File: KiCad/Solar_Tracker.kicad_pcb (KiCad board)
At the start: 2 copper layers, 160 x 100 mm, 116 parts, among them J1 +48V, J10 AZJMP, J11 ELJMP, J12 AZ, J13 CONN_01X03, J2 HOLE, J3 HOLE, J4 EL, J5 HOLE, J6 HOLE, J7 CONN_01X05, J8 GPIO, J9 GPIO, Q1 BUK9M42-60E, Q2 BUK9M42-60E, Q3 BUK9M42-60E, Q4 BUK9M42-60E, Q5 BUK9M42-60E, Q6 BUK9M42-60E, Q7 BUK9M42-60E, Q8 BUK9M42-60E, U1 MER1S4805SC, U10 TLP291, U11 75LBC182, U12 A4927, U2 A4927, U3 Nano, U4 A4927, U5 A4927, U6 MER1S4805SC, U7 TLP291, U8 TLP291, U9 TLP291

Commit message: Imported netlist
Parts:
- U12, U2, U4, U5: footprint Housings_SSOP:ST_PowerSSO-24_SlugDown_ThermalVias -> SOLAR:TSSOP-24_4.4x7.8mm_Pitch0.65mm
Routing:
- net GND: track 160.9 -> 142.9 mm
- net (no net): track 183.3 -> 192.8 mm
- net Net-(U5-Pad14): track 0.00 -> 3.21 mm
- net Net-(U2-Pad14): track 0.00 -> 2.20 mm
- net Net-(U12-Pad14): track 0.00 -> 1.56 mm
- net Net-(U4-Pad14): track 0.00 -> 1.43 mm

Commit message: Fixed connectors
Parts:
- J1, J12, J4, J8, J9: footprint Connectors_Phoenix:PhoenixContact_GMSTBA-G_02x7.50mm_Angled -> Connectors_Phoenix:PhoenixContact_GMSTBVA-G_02x7.50mm_Vertical
- J13: footprint Connectors_Phoenix:PhoenixContact_GMSTBA-G_03x7.50mm_Angled -> Connectors_Phoenix:PhoenixContact_MCV-G_03x5.08mm_Vertical
- J7: footprint Connectors_Phoenix:PhoenixContact_GMSTBA-G_05x7.50mm_Angled -> Connectors_Phoenix:PhoenixContact_MCV-G_05x5.08mm_Vertical
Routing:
- net GND: track 142.9 -> 156.3 mm
- net A7: track 63.6 -> 50.2 mm

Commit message: Added expander to pcb
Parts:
- added C33: 1u, Capacitors_SMD:C_1206_HandSoldering, F.Cu at (69.8, 133.3)
- added R33: 1K, Resistors_SMD:R_1206_HandSoldering, F.Cu at (78.7, 128.3)
- added R34: 1K, Resistors_SMD:R_1206_HandSoldering, F.Cu at (78.7, 121.9)
- added R37: 1K, Resistors_SMD:R_1206_HandSoldering, F.Cu at (78.7, 115.6)
- added R38: 1K, Resistors_SMD:R_1206_HandSoldering, F.Cu at (88.9, 116.8)
- added R42: 1K, Resistors_SMD:R_1206_HandSoldering, F.Cu at (87.6, 121.9)
- added U13: PCA9685, Housings_SSOP:TSSOP-28_4.4x9.7mm_Pitch0.65mm, F.Cu at (66.0, 121.9)
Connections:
- U3 pad 11: ELBL -> Net-(U3-Pad11)
- U3 pad 12: ELBH -> Net-(U3-Pad12)
- U3 pad 13: AZBL -> Net-(U3-Pad13)
- U3 pad 14: AZBH -> Net-(U3-Pad14)
- U3 pad 23: TLED -> Net-(R34-Pad2)
- U3 pad 24: RLED -> Net-(U13-Pad26)
- U3 pad 5: AZFL -> Net-(U3-Pad5)
- U3 pad 6: AZFH -> Net-(U3-Pad6)
- U3 pad 7: ELFL -> Net-(U3-Pad7)
- U3 pad 8: ELFH -> Net-(U3-Pad8)
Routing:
- net Net-(U3-Pad14): track 0.00 -> 195.2 mm
- net AZBH: track 195.2 -> 0.00 mm
- net Net-(U3-Pad13): track 0.00 -> 190.4 mm
- net AZBL: track 190.4 -> 0.00 mm
- net Net-(U3-Pad12): track 0.00 -> 158.8 mm
- net ELBH: track 158.8 -> 0.00 mm
- net Net-(U3-Pad11): track 0.00 -> 154.1 mm
- net ELBL: track 154.1 -> 0.00 mm
- net Net-(U3-Pad8): track 0.00 -> 43.7 mm
- net ELFH: track 43.7 -> 0.00 mm
- net Net-(U3-Pad7): track 0.00 -> 42.1 mm
- net ELFL: track 42.1 -> 0.00 mm
- net Net-(U3-Pad6): track 0.00 -> 41.7 mm
- net AZFH: track 41.7 -> 0.00 mm
- net Net-(U3-Pad5): track 0.00 -> 38.8 mm
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
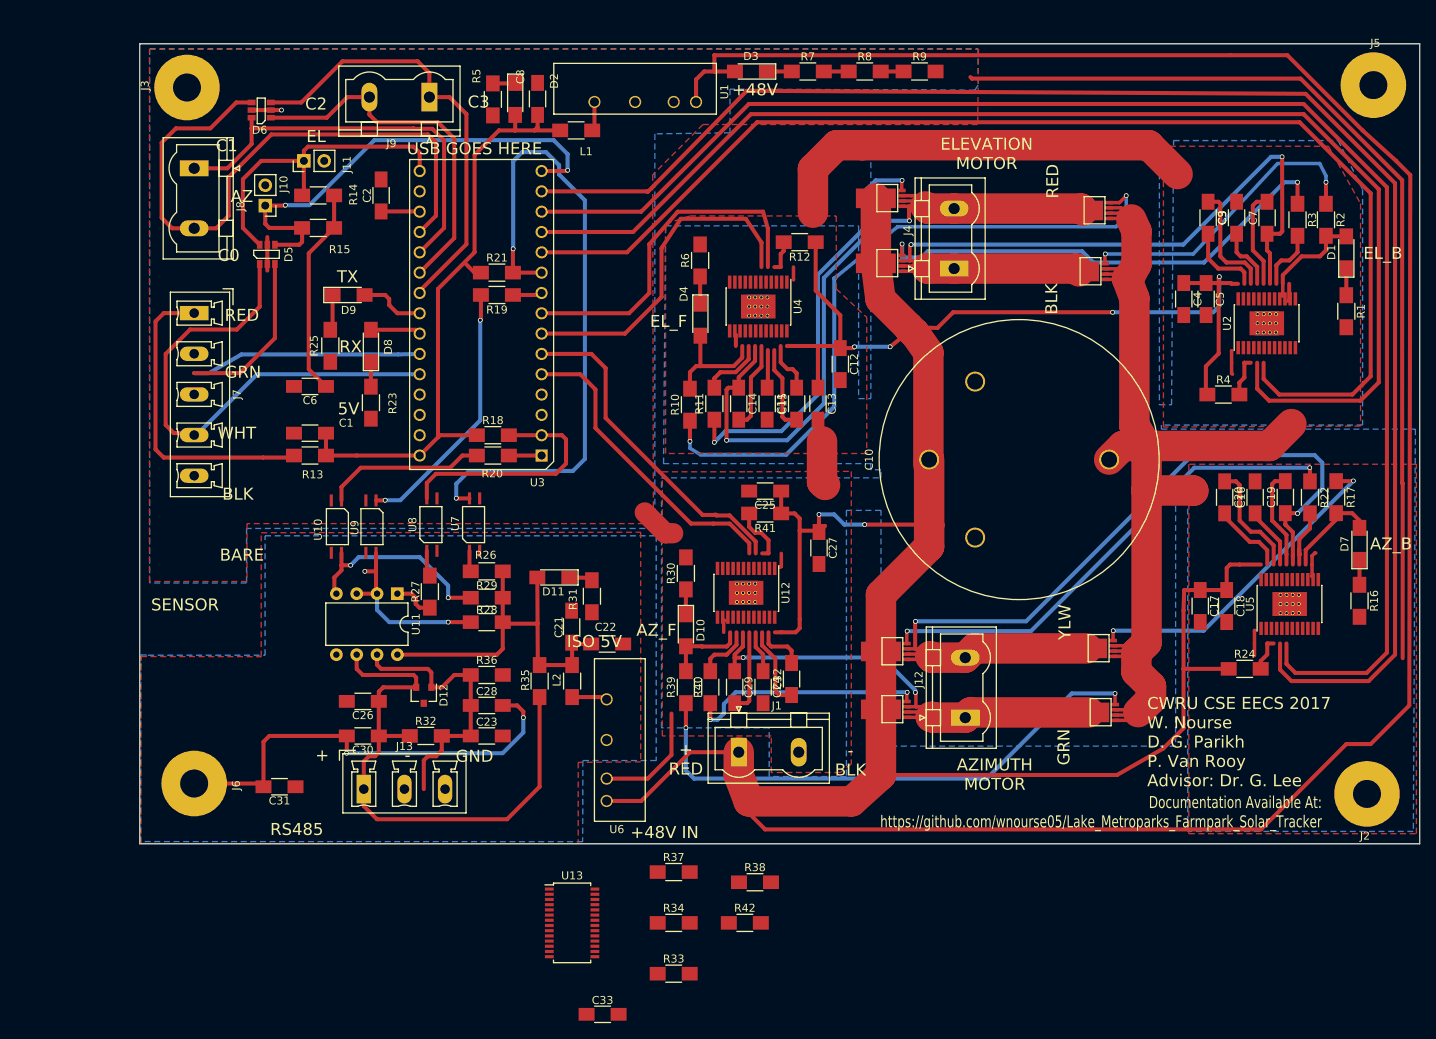
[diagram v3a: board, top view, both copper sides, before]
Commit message: updates to layout due to new footprints. Gave space to power, fixed connectors, began motors
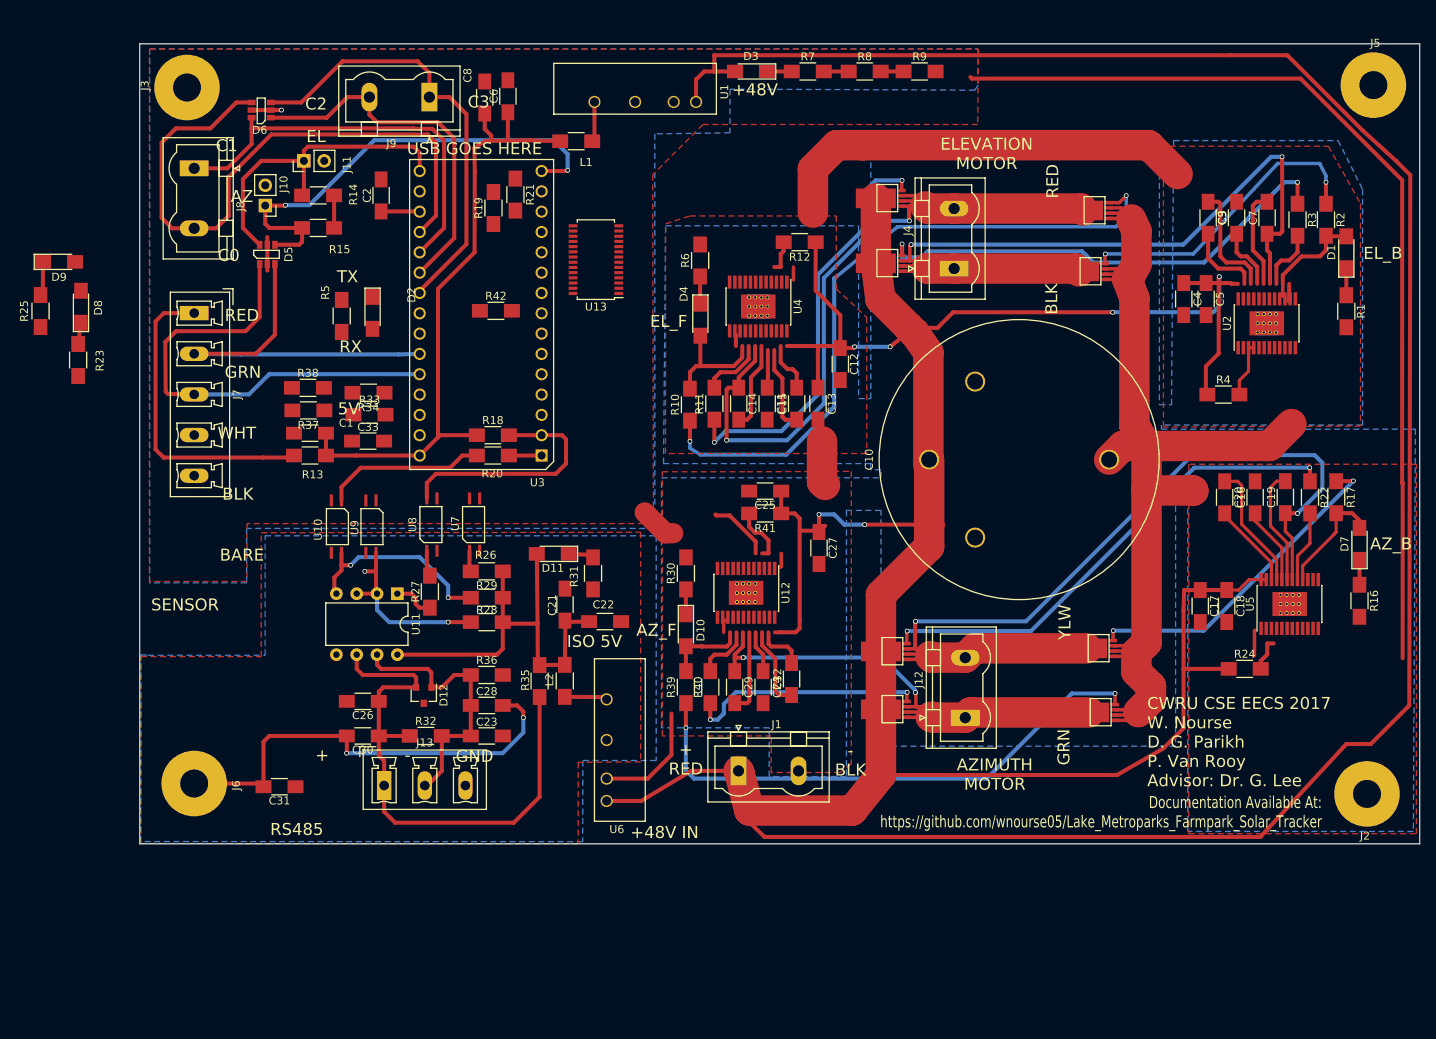
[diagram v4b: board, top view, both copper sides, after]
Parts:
- moved R38 83.3 mm to (33.0, 55.0)
- moved U13 83.0 mm to (69.0, 39.0), turned to 180 degrees
- moved R42 82.6 mm to (56.5, 45.4)
- moved R33 79.6 mm to (40.7, 58.4)
- moved C33 77.4 mm to (40.5, 61.7)
- moved R34 76.5 mm to (40.6, 55.7), turned to 180 degrees
- moved R37 73.6 mm to (33.1, 57.9), turned to 180 degrees
- moved C6 43.9 mm to (58.0, 18.6), turned to 90 degrees
- moved R23 37.0 mm to (4.29, 51.6)
- moved D8 36.6 mm to (4.65, 44.9)
- moved R25 36.5 mm to (-0.41, 45.4)
- moved D9 36.4 mm to (1.91, 39.3)
- moved R5 33.0 mm to (37.2, 46.1)
- moved D2 32.1 mm to (41.1, 45.7)
- moved R19 10.9 mm to (56.2, 32.6), turned to 90 degrees
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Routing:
- net Net-(U3-Pad14): track 195.2 -> 0.00 mm
- net Net-(U3-Pad13): track 190.4 -> 0.00 mm
- net Net-(U3-Pad12): track 158.8 -> 0.00 mm
- net Net-(U3-Pad11): track 154.1 -> 0.00 mm
- net ISO_PWR_DET: track 83.3 -> 0.00 mm, vias 2 -> 0
- net Net-(U3-Pad8): track 43.7 -> 0.00 mm
- net Net-(U3-Pad7): track 42.1 -> 0.00 mm
- net Net-(U3-Pad6): track 41.7 -> 0.00 mm
- net Net-(U3-Pad5): track 38.8 -> 0.00 mm
- net Net-(R19-Pad2): track 32.9 -> 0.00 mm, vias 2 -> 0
- net +5V: track 104.3 -> 83.1 mm
- net GND: track 156.3 -> 143.4 mm
- net A7: track 50.2 -> 58.9 mm
- net +48V: track 613.7 -> 606.7 mm
- net RLED: track 5.62 -> 0.00 mm
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
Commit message: continued with motors and new layout
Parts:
- moved D2 13.1 mm to (30.2, 52.9), turned to 0 degrees
- moved R5 12.0 mm to (30.2, 55.8), turned to 0 degrees
- moved R37 12.0 mm to (40.3, 48.3), turned to 0 degrees
- moved R42 11.6 mm to (55.9, 57.0)
- moved R19 10.5 mm to (57.0, 43.1), turned to 180 degrees
- moved R21 9.62 mm to (58.0, 40.5), turned to 0 degrees
- moved R38 7.74 mm to (40.5, 52.9), turned to 180 degrees
- moved U13 3.36 mm to (69.8, 35.8)
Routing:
- net Net-(R34-Pad2): track 0.00 -> 93.8 mm, vias 0 -> 4
- net Net-(U13-Pad26): track 0.00 -> 85.6 mm, vias 0 -> 1
- net +5V: track 83.1 -> 139.7 mm
- net Net-(R42-Pad2): track 0.00 -> 48.6 mm, vias 0 -> 2
- net GND: track 143.4 -> 188.2 mm
- net ISO_PWR_DET: track 0.00 -> 39.1 mm, vias 0 -> 2
- net Net-(R19-Pad2): track 0.00 -> 35.0 mm, vias 0 -> 2
- net (no net): track 197.8 -> 173.0 mm
- net AZRTE: track 59.6 -> 53.7 mm
- net Net-(R37-Pad2): track 0.00 -> 4.66 mm
- net EN: track 0.00 -> 3.27 mm
- net Net-(D2-Pad1): track 0.00 -> 2.92 mm
- net Net-(R33-Pad2): track 0.00 -> 2.80 mm
- net Net-(C15-Pad1): track 10.7 -> 13.4 mm
- net Net-(C11-Pad1): track 4.74 -> 7.15 mm
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
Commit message: Same stuff, different day
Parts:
- removed D8: RX, LEDs:LED_1206_HandSoldering
- removed D9: TX, LEDs:LED_1206_HandSoldering
- removed R23, R25: 150, Resistors_SMD:R_1206_HandSoldering
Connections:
- R38 pad 2: Net-(R34-Pad2) -> Net-(R38-Pad2)
- U13 pad 10: AZFL -> ELBL
- U13 pad 11: AZFH -> ELBH
- U13 pad 12: ELFL -> AZBL
- U13 pad 13: ELFH -> AZBH
- U13 pad 26: Net-(U13-Pad26) -> Net-(R38-Pad2)
- U13 pad 6: ELBL -> AZFL
- U13 pad 7: ELBH -> AZFH
- U13 pad 8: AZBL -> ELFL
- U13 pad 9: AZBH -> ELFH
- U3 pad 14: Net-(U3-Pad14) -> Net-(R42-Pad2)
- U3 pad 24: Net-(U13-Pad26) -> Net-(R38-Pad2)
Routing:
- net Net-(R38-Pad2): track 0.00 -> 88.4 mm, vias 0 -> 1
- net Net-(U13-Pad26): track 85.6 -> 0.00 mm, vias 1 -> 0
- net (no net): track 173.0 -> 179.9 mm
- net Net-(D9-Pad1): track 4.27 -> 0.00 mm
- net Net-(R34-Pad2): track 93.8 -> 91.0 mm
- net Net-(D8-Pad1): track 2.68 -> 0.00 mm

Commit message: Reintegration
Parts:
- moved R5 54.1 mm to (75.0, 25.5), turned to 90 degrees
- moved D2 47.9 mm to (69.8, 26.0), turned to 180 degrees
- moved R42 28.9 mm to (59.4, 28.4), turned to 270 degrees
- moved R33 12.5 mm to (35.5, 47.0), turned to 180 degrees
- moved R38 12.3 mm to (35.6, 41.6), turned to 0 degrees
- moved R34 7.87 mm to (35.6, 49.6), turned to 0 degrees
- moved R37 6.25 mm to (35.5, 44.2), turned to 180 degrees
- moved L1 1.12 mm to (66.5, 23.1)
- moved C32 0.74 mm to (93.5, 92.2)
- moved R6 0.43 mm to (82.1, 39.5)
- moved J5 0.34 mm to (166.5, 17.4)
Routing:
- net GND: track 188.2 -> 378.5 mm
- net AZBH: track 0.00 -> 181.8 mm
- net (no net): track 179.9 -> 0.00 mm
- net AZBL: track 0.00 -> 176.7 mm
- net ELBH: track 0.00 -> 148.0 mm
- net ELBL: track 0.00 -> 144.0 mm
- net +5V: track 139.7 -> 223.5 mm
- net AZFH: track 0.00 -> 49.6 mm
- net AZFL: track 0.00 -> 48.3 mm
- net Net-(R42-Pad2): track 48.6 -> 11.9 mm, vias 2 -> 1
- net ELFH: track 0.00 -> 23.9 mm
- net ELFL: track 0.00 -> 22.9 mm
- net Net-(R38-Pad2): track 88.4 -> 97.8 mm
- net Net-(R34-Pad2): track 91.0 -> 83.4 mm, vias 4 -> 1
- net +48V: track 608.6 -> 601.7 mm
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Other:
- board text added: "CWRU CSE EECS 2017 Advisor: Dr. G. Lee Documentation at:"
- board text added: "https://github.com/FarmparkSolarTracker/Lake_Metroparks_Farmpark_Solar_Tracker/wiki Copyright © 2017 W. Nourse, D. G. Parikh, P. Van Rooy"
- board text removed: "CWRU CSE EECS 2017 W. Nourse D. G. Parikh P. Van Rooy Advisor: Dr. G. Lee"
- board text removed: "Documentation Available At: https://github.com/wnourse05/Lake_Metroparks_Farmpark_Solar_Tracker"
- board text removed: "RX"
- board text removed: "TX"

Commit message: Updated documentation
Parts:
- added D13: STAT2, LEDs:LED_1206_HandSoldering, F.Cu at (79.0, 67.1)
- added D14: STAT1, LEDs:LED_1206_HandSoldering, F.Cu at (79.0, 63.5)
- added D15: TVS_x4, SOLAR:tvs_quad, F.Cu at (57.9, 58.2)
- added D16: TVS_x4, SOLAR:tvs_quad, F.Cu at (58.3, 38.1)
- added D8: STAT4, LEDs:LED_1206_HandSoldering, F.Cu at (79.0, 74.2)
- added D9: STAT3, LEDs:LED_1206_HandSoldering, F.Cu at (79.0, 70.6)
- added F1: Fuse, Resistors_THT:R_Axial_DIN0204_L3.6mm_D1.6mm_P5.08mm_Horizontal, F.Cu at (109.7, 103.1)
- added R23: 150, Resistors_SMD:R_0805, F.Cu at (73.4, 74.2)
- added R25: 150, Resistors_SMD:R_0805, F.Cu at (73.4, 70.6)
- added R43: 150, Resistors_SMD:R_0805, F.Cu at (73.4, 63.5)
- added R44: 1K, Resistors_SMD:R_0805, F.Cu at (54.6, 41.7)
- added R45: 1K, Resistors_SMD:R_0805, F.Cu at (54.6, 35.3)
- added R46: 1K, Resistors_SMD:R_0805, F.Cu at (57.8, 33.4)
- added R47: 1K, Resistors_SMD:R_0805, F.Cu at (67.2, 31.8)
- added SW1: DIPSWITCH, Housings_DIP:DIP-12_W7.62mm, F.Cu at (78.5, 44.3)
- added TP1: +48V, SOLAR:test_pad, F.Cu at (111.8, 106.2)
- added TP10: AZBH, SOLAR:test_pad, F.Cu at (158.0, 89.5)
- added TP11: RX, SOLAR:test_pad, F.Cu at (65.2, 67.3)
- added TP12: TX, SOLAR:test_pad, F.Cu at (61.7, 76.5)
- added TP13: +5V_ISO, SOLAR:test_pad, F.Cu at (58.2, 87.6)
- added TP2: +5V, SOLAR:test_pad, F.Cu at (69.1, 19.6)
- added TP3: AZFL, SOLAR:test_pad, F.Cu at (93.0, 74.7)
- added TP4: AZFH, SOLAR:test_pad, F.Cu at (95.2, 74.7)
- added TP5: ELFL, SOLAR:test_pad, F.Cu at (96.9, 29.3)
- added TP6: ELFH, SOLAR:test_pad, F.Cu at (99.2, 29.5)
- added TP7: ELBL, SOLAR:test_pad, F.Cu at (158.5, 54.1)
- added TP8: ELBH, SOLAR:test_pad, F.Cu at (156.2, 54.0)
- added TP9: AZBL, SOLAR:test_pad, F.Cu at (160.5, 89.5)
- C1, C11, C12, C13, C14, C15, C16, C17, C18, C19, C2, C20, C21, C22, C23, C24, C25, C26, C27, C28, C29, C3, C30, C31, C32, C33, C4, C5, C6, C7, C8, C9: footprint Capacitors_SMD:C_1206_HandSoldering -> Capacitors_SMD:C_0805
- C10: footprint SOLAR_TRACKER:vnd_cap -> SOLAR:vnd_cap
- D5, D6: footprint SOLAR_TRACKER:tvs_quad -> SOLAR:tvs_quad
- J10: value AZJMP -> GPIO; footprint Pin_Headers:Pin_Header_Straight_1x02_Pitch2.54mm -> Connectors_Phoenix:PhoenixContact_GMSTBVA-G_02x7.50mm_Vertical
- J11: value ELJMP -> GPIO; footprint Pin_Headers:Pin_Header_Straight_1x02_Pitch2.54mm -> Connectors_Phoenix:PhoenixContact_GMSTBVA-G_02x7.50mm_Vertical
- J2, J3, J5, J6: footprint SOLAR_TRACKER:M3 -> SOLAR:M3
- Q1, Q2, Q3, Q4, Q5, Q6, Q7, Q8: footprint SOLAR_TRACKER:nFET -> SOLAR:nFET
- R1, R10, R11, R12, R13, R14, R15, R16, R17, R18, R19, R2, R20, R21, R22, R24, R26, R27, R28, R29, R3, R30, R31, R32, R33, R34, R35, R36, R37, R38, R39, R4, R40, R41, R5, R6, R7, R8, R9: footprint Resistors_SMD:R_1206_HandSoldering -> Resistors_SMD:R_0805
- R42: value 1K -> 150; footprint Resistors_SMD:R_1206_HandSoldering -> Resistors_SMD:R_0805
- U1, U6: footprint SOLAR_TRACKER:5v_iso -> SOLAR:5v_iso
- U10, U7, U8, U9: footprint SOLAR_TRACKER:opto -> SOLAR:opto
- U3: footprint SOLAR_TRACKER:nano -> Modules:Arduino_Nano
- moved R16 94.5 mm to (73.4, 56.4), turned to 180 degrees
- moved R1 89.5 mm to (73.4, 49.8), turned to 180 degrees
- moved D7 87.4 mm to (79.0, 56.4), turned to 0 degrees
- moved D1 84.6 mm to (79.0, 49.8), turned to 0 degrees
- moved J11 77.6 mm to (70.7, 94.2), turned to 0 degrees
- moved J10 72.0 mm to (78.4, 83.4)
- moved R42 41.1 mm to (73.4, 67.1), turned to 180 degrees
- moved U13 33.5 mm to (92.5, 60.5)
- moved D10 25.4 mm to (79.0, 59.9), turned to 0 degrees
- moved R14 21.6 mm to (31.2, 52.3), turned to 270 degrees
- moved C25 20.4 mm to (104.3, 82.7), turned to 90 degrees
- moved R30 19.5 mm to (73.4, 59.9), turned to 180 degrees
- moved C13 19.4 mm to (106.3, 40.1)
- moved R10 18.2 mm to (94.2, 45.0)
- moved R11 17.3 mm to (96.3, 45.0)
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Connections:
- net C0 renamed G0
- net C1 renamed G1
- net C2 renamed G2
- net C3 renamed G3
- D5 pad 4: AZRTE -> SEL0
- D5 pad 6: ELRTE -> SEL1
- J1 pad 1: +48V -> Net-(F1-Pad2)
- J10 pad 1: AZRTE -> G5
- J10 pad 2: GND -> G4
- J11 pad 1: ELRTE -> G7
- J11 pad 2: GND -> G6
- R10 pad 2: Net-(D4-Pad2) -> Net-(R10-Pad2)
- R14 pad 1: ELRTE -> SEL0
- R15 pad 1: AZRTE -> SEL1
- R17 pad 2: Net-(D7-Pad2) -> Net-(R17-Pad2)
- R2 pad 2: Net-(D1-Pad2) -> Net-(R2-Pad2)
- R39 pad 2: Net-(D10-Pad2) -> Net-(R39-Pad2)
- R42 pad 1: +5V -> Net-(D13-Pad1)
- R42 pad 2: Net-(R42-Pad2) -> GND
- U12 pad 16: Net-(D10-Pad2) -> Net-(R39-Pad2)
- U13 pad 1: +5V -> GND
- U13 pad 15: Net-(U13-Pad15) -> Net-(D1-Pad2)
- U13 pad 16: Net-(U13-Pad16) -> Net-(D4-Pad2)
- U13 pad 17: Net-(U13-Pad17) -> Net-(D7-Pad2)
- U13 pad 18: Net-(U13-Pad18) -> Net-(D10-Pad2)
- U13 pad 23: Net-(R42-Pad2) -> GND
- U13 pad 26: Net-(R38-Pad2) -> Net-(R34-Pad2)
- U13 pad 27: Net-(R34-Pad2) -> Net-(R38-Pad2)
- U13 pad 3: +5V -> GND
- U13 pad 5: +5V -> GND
- U2 pad 16: Net-(D1-Pad2) -> Net-(R2-Pad2)
- U3 pad 11: Net-(U3-Pad11) -> SEL0
- U3 pad 12: Net-(U3-Pad12) -> SEL1
- U3 pad 13: Net-(U3-Pad13) -> SEL2
- U3 pad 14: Net-(R42-Pad2) -> SEL3
- U3 pad 15: AZRTE -> SEL4
- U3 pad 16: ELRTE -> SEL5
- U3 pad 23: Net-(R34-Pad2) -> Net-(R38-Pad2)
- U3 pad 24: Net-(R38-Pad2) -> Net-(R34-Pad2)
- U3 pad 5: Net-(U3-Pad5) -> G4
- U3 pad 6: Net-(U3-Pad6) -> G5
- U3 pad 7: Net-(U3-Pad7) -> G6
- U3 pad 8: Net-(U3-Pad8) -> G7
- U4 pad 16: Net-(D4-Pad2) -> Net-(R10-Pad2)
- U5 pad 16: Net-(D7-Pad2) -> Net-(R17-Pad2)
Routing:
- net SEL5: track 0.00 -> 110.7 mm, vias 0 -> 3
- net G7: track 0.00 -> 86.3 mm
- net SEL0: track 0.00 -> 83.8 mm, vias 0 -> 1
- net SEL1: track 0.00 -> 67.4 mm, vias 0 -> 1
- net G6: track 0.00 -> 64.1 mm
- net AZRTE: track 53.9 -> 0.00 mm, vias 2 -> 0
- net G5: track 0.00 -> 40.7 mm
- net ELRTE: track 40.6 -> 0.00 mm
- net +48V: track 601.7 -> 563.2 mm
- net ELFH: track 23.9 -> 59.2 mm
- net +5V: track 223.5 -> 258.0 mm
- net GND: track 378.5 -> 346.1 mm, vias 1 -> 15
- net G4: track 0.00 -> 31.4 mm
- net AZ_B: track 108.3 -> 77.7 mm
- net ELFL: track 22.9 -> 51.6 mm
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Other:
- board text added: "G4"
- board text added: "G5"
- board text added: "G6"
- board text added: "G7"
- board text added: "https://github.com/FarmparkSolarTracker/Lake_Metroparks_Farmpark_Solar_Tracker/wiki Copyright © 2018 W. Nourse, D. G. Parikh, P. Van Rooy"
- board text removed: "https://github.com/FarmparkSolarTracker/Lake_Metroparks_Farmpark_Solar_Tracker/wiki Copyright © 2017 W. Nourse, D. G. Parikh, P. Van Rooy"
